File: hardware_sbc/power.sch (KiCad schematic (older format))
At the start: 49 parts, among them J6 Conn_01x02, J7 S2B-PH-K-S(LF)(SN), J8 Conn_01x01_Male, J9 0874380343, U10 MIC94164, U5 MP2636GR-P, U6 NCP133AMX150TCG

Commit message: Clean up bom and add config for KiBoM
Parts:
- D3, D4, D5: Part (none) -> 150060GS75000; Vendor 732-4971-1-ND -> (none); Vendorpart 150060GS75000 -> 732-4971-1-ND
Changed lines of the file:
@@
 F 2 "LED_SMD:LED_0603_1608Metric" H 6600 6850 50  0001 C CNN
 F 3 "~" H 6600 6850 50  0001 C CNN
-F 4 "732-4971-1-ND" H 6600 6850 50  0001 C CNN "Vendor"
-F 5 "150060GS75000" H 6593 6686 50  0001 C CNN "Vendorpart"
-F 6 "Wurth" H 6600 6850 50  0001 C CNN "Mfgr"
-F 7 "DNP" H 6600 6950 50  0000 C CNN "Populate"
+F 4 "732-4971-1-ND" H 6593 6686 50  0001 C CNN "Vendorpart"
+F 5 "Wurth" H 6600 6850 50  0001 C CNN "Mfgr"
+F 6 "DNP" H 6600 6950 50  0000 C CNN "Populate"
+F 7 "150060GS75000" H 6600 6850 50  0001 C CNN "Part"
 	1    6600 6850
 	-1   0    0    1
@@
 F 2 "LED_SMD:LED_0603_1608Metric" H 6600 7050 50  0001 C CNN
 F 3 "~" H 6600 7050 50  0001 C CNN
-F 4 "732-4971-1-ND" H 6600 7050 50  0001 C CNN "Vendor"
-F 5 "150060GS75000" H 6593 6795 50  0001 C CNN "Vendorpart"
-F 6 "Wurth" H 6600 7050 50  0001 C CNN "Mfgr"
-F 7 "DNP" H 6600 7150 50  0000 C CNN "Populate"
+F 4 "732-4971-1-ND" H 6593 6795 50  0001 C CNN "Vendorpart"
+F 5 "Wurth" H 6600 7050 50  0001 C CNN "Mfgr"
+F 6 "DNP" H 6600 7150 50  0000 C CNN "Populate"
+F 7 "150060GS75000" H 6600 7050 50  0001 C CNN "Part"
 	1    6600 7050
 	-1   0    0    1
@@
 F 2 "LED_SMD:LED_0603_1608Metric" H 6600 6650 50  0001 C CNN
 F 3 "~" H 6600 6650 50  0001 C CNN
-F 4 "732-4971-1-ND" H 6600 6650 50  0001 C CNN "Vendor"
-F 5 "150060GS75000" H 6593 6486 50  0001 C CNN "Vendorpart"
-F 6 "Wurth" H 6600 6650 50  0001 C CNN "Mfgr"
+F 4 "732-4971-1-ND" H 6593 6486 50  0001 C CNN "Vendorpart"
+F 5 "Wurth" H 6600 6650 50  0001 C CNN "Mfgr"
+F 6 "150060GS75000" H 6600 6650 50  0001 C CNN "Part"
 	1    6600 6650
 	-1   0    0    1

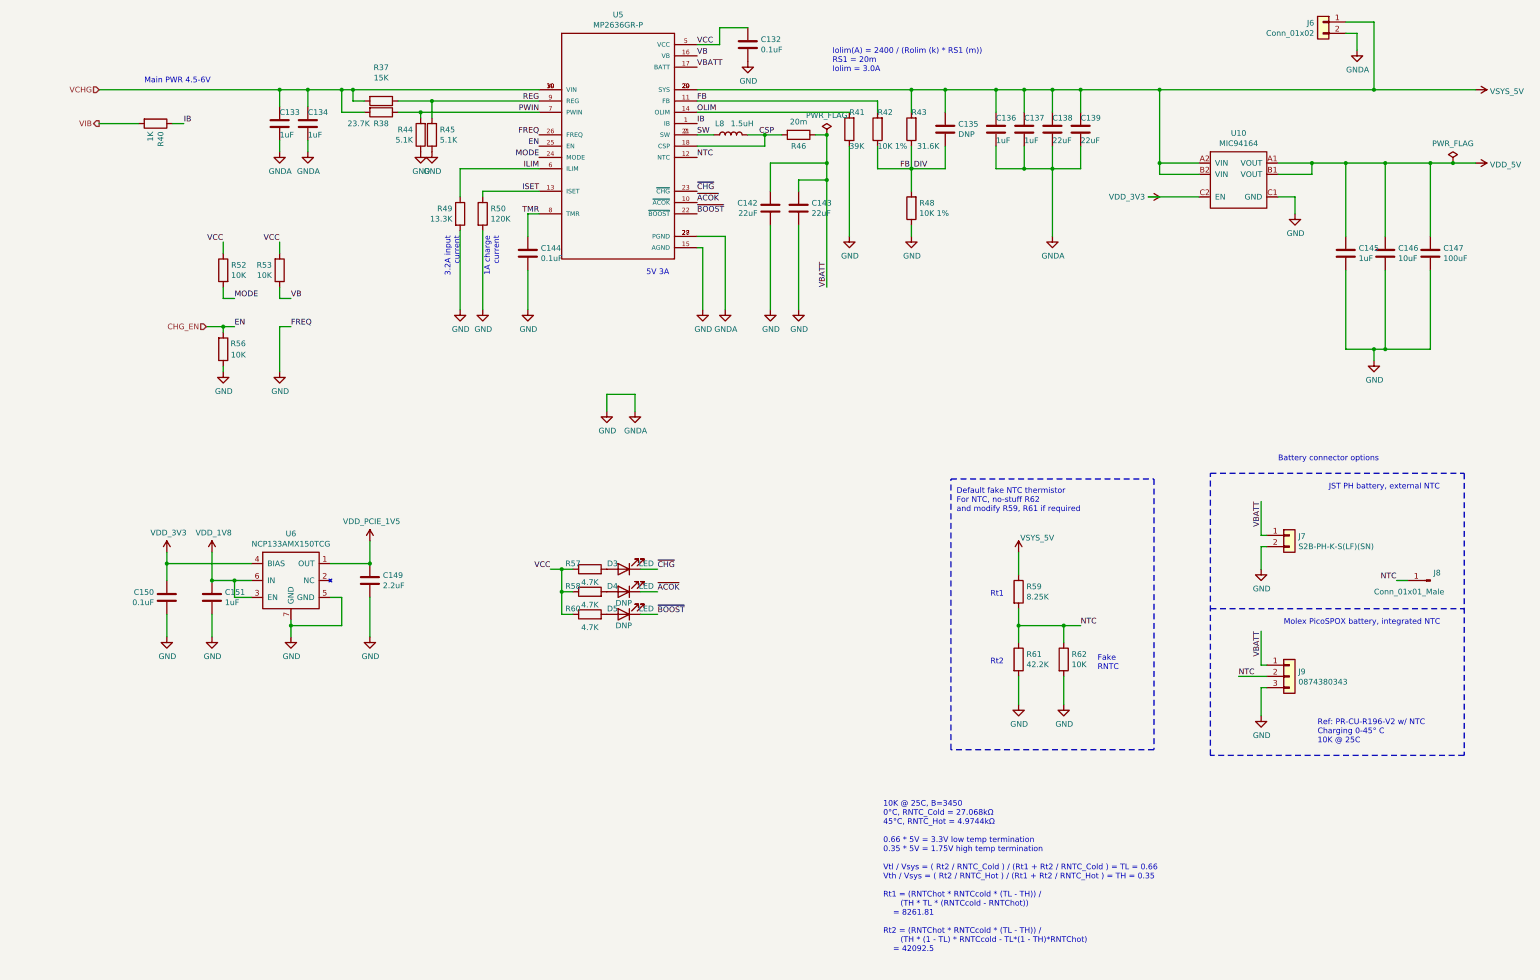
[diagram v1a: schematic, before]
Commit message: Add battery monitor and protection circuit
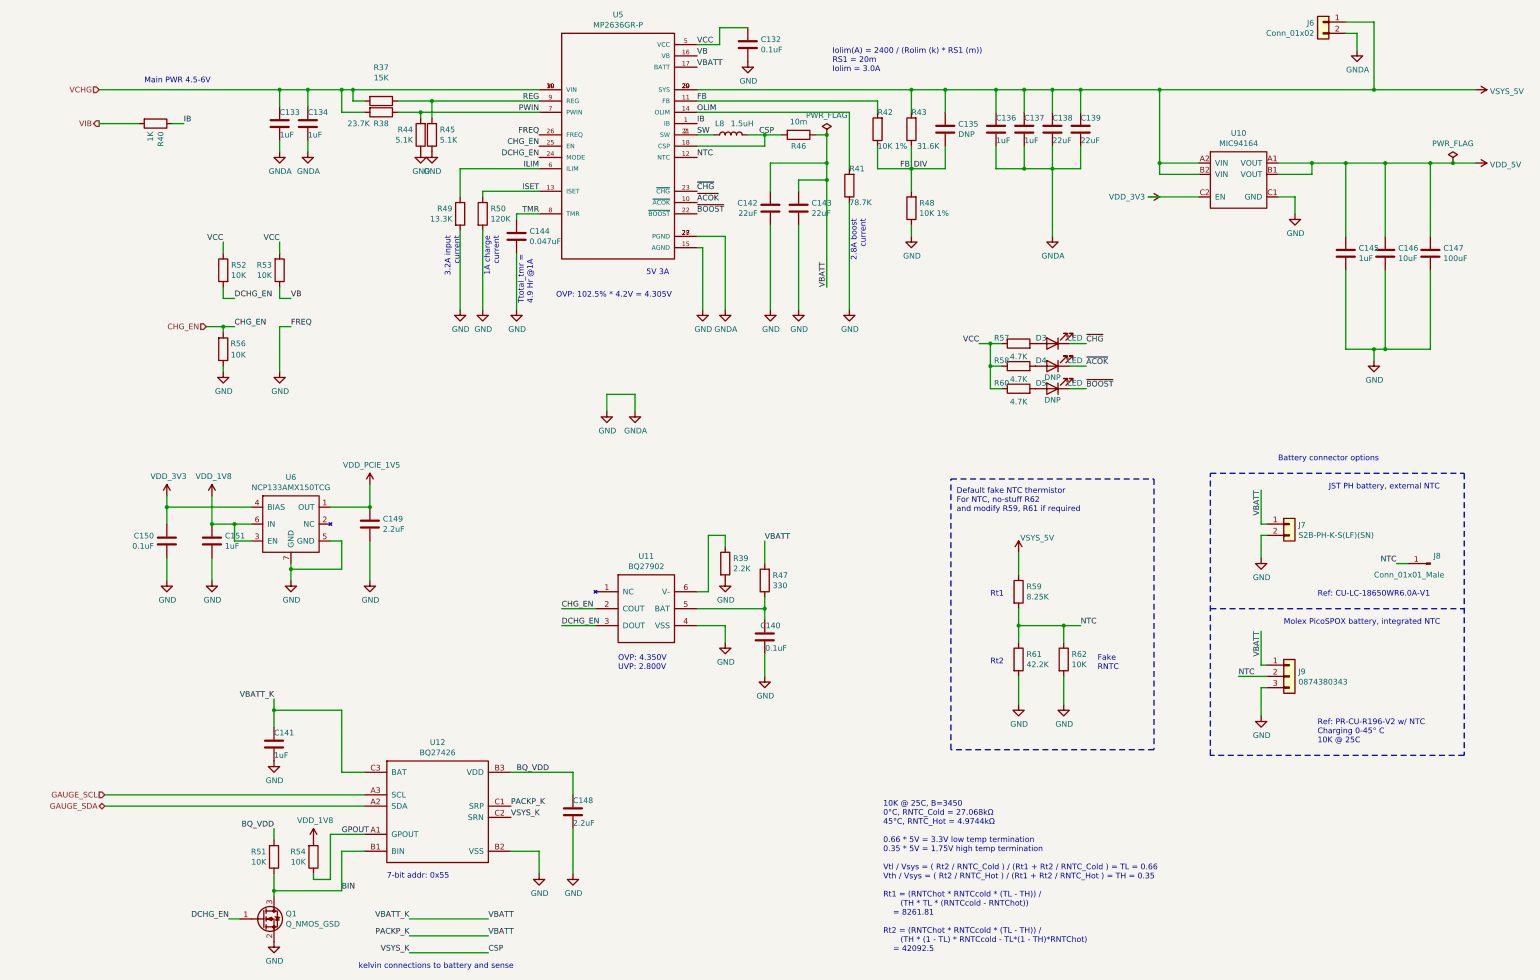
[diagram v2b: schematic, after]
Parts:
- added C140: 0.1uF, Capacitor_SMD:C_0201_0603Metric, symbol Device:C
- added C141: 1uF, Capacitor_SMD:C_0402_1005Metric, symbol Device:C
- added C148: 2.2uF, Capacitor_SMD:C_0201_0603Metric, symbol Device:C
- added Q1: Q_NMOS_GSD, Package_DFN_QFN:Diodes_DFN1006-3, symbol Device:Q_NMOS_GSD
- added R39: 2.2K, Resistor_SMD:R_0201_0603Metric, symbol Device:R
- added R47: 330, Resistor_SMD:R_0201_0603Metric, symbol Device:R
- added R51, R54: 10K, Resistor_SMD:R_0201_0603Metric, symbol Device:R
- added U11: BQ27902, Package_SON:WSON-6_1.5x1.5mm_P0.5mm, symbol mxenc:BQ279XX
- added U12: BQ27426, Package_BGA:BGA-9_1.6x1.6mm_Layout3x3_P0.5mm, symbol mxenc:BQ27426
- C144: value 0.1uF -> 0.047uF; Part GRM155R71E104KE14J -> GRM155R71A473KA01D; Vendorpart 490-14603-1-ND -> 490-1316-1-ND
- R41: value 39K -> 78.7K; Part RC0201FR-0739KL -> RC0201FR-0778R7L; Vendorpart YAG2641CT-ND -> YAG2803CT-ND
- R46: value 20m -> 10m; Part ERJ-8CWFR020V -> ERJ-8CWFR010V; Vendorpart P0.02BVCT-ND -> P0.01BVCT-ND
- R50: Part AC0201FR-07120KL -> AC0201FR-07240KL; Vendorpart YAG5150CT-ND -> YAG5179CT-ND
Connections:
- net CHG_EN: now also U11.2 (COUT)
- net CSP: now also U12.C2 (SRN)
- net GND: now also C140.2, C141.2, C148.2, Q1.2 (S), R39.2, U11.4 (VSS), U12.B2 (VSS)
- net VDD_1V8: now also R54.2
- net MODE renamed DCHG_EN
- net DCHG_EN: now also Q1.1 (G), U11.3 (DOUT)
- net VBATT renamed PACKP_K
- net PACKP_K: now also C141.1, R47.2, U12.C1 (SRP), U12.C3 (BAT)
- new net: C140.1, R47.1, U11.5 (BAT)
- new net: R39.1, U11.6 (V-)
- new net BIN: Q1.3 (D), R51.1, U12.B1 (BIN)
- new net BQ_VDD: C148.1, R51.2, U12.B3 (VDD)
- new net GAUGE_SCL: U12.A3 (SCL)
- new net GAUGE_SDA: U12.A2 (SDA)
- new net GPOUT: R54.1, U12.A1 (GPOUT)
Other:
- note added: "2.8A boost\ncurrent"
- note added: "7-bit addr: 0x55"
- note added: "OVP: 102.5% * 4.2V = 4.305V"
- note added: "OVP: 4.350V\nUVP: 2.800V"
- note added: "Ref: CU-LC-18650WR6.0A-V1"
- note added: "Ttotal_tmr =\n4.9 Hr @1A"
- note added: "kelvin connections to battery and sense"
- moved on the sheet: C144, C149, C150, C151, D3, D4, D5, J7, J8, R41, R57, R58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

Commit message: BOM and misc fixes for production of 0.9 boards
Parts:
- C132: Mfgrpart (none) -> GRM155R71E104KE14J; Part GRM155R71E104KE14J -> (none)
- C133, C134, C136, C137, C141, C145, C151: Mfgrpart (none) -> GRM155C81A105KA12D; Part GRM155C81A105KA12D -> (none)
- C138, C139, C142, C143: Mfgrpart (none) -> GRM188C80G226MEA0D; Part GRM188C80G226MEA0D -> (none)
- C140, C150: Mfgrpart (none) -> GRM033C80J104KE15D; Part GRM033C80J104KE15D -> (none)
- C144: Mfgrpart (none) -> GRM155R71A473KA01D; Part GRM155R71A473KA01D -> (none)
- C146: Mfgrpart (none) -> CL21X106KPYNNNE; Part CL21X106KPYNNNE -> (none)
- C147: Mfgrpart (none) -> GRM32EC70J107ME15L; Part GRM32EC70J107ME15L -> (none)
- C148: Mfgrpart (none) -> GRM033D80E225ME47D; Part GRM033D80E225ME47D -> (none)
- C149: Mfgrpart (none) -> GRM155C80J225ME95D; Part GRM155C80J225ME95D -> (none)
- D3, D4, D5: Mfgrpart (none) -> 150060GS75000; Part 150060GS75000 -> (none)
- J7: Mfgrpart (none) -> S2B-PH-K-S(LF)(SN); Part S2B-PH-K-S(LF)(SN) -> (none)
- J9: Mfgrpart (none) -> 0874380343; Part 0874380343 -> (none)
- L8: Mfgrpart (none) -> 74438357015; Part 74438357015 -> (none)
- Q1: Mfgrpart (none) -> NX7002BKMB; Part NX7002BKMB -> (none)
- R37: Mfgrpart (none) -> RC0201FR-0715KL; Part RC0201FR-0715KL -> (none)
- R38: Mfgrpart (none) -> RC0201FR-0723K7L; Part RC0201FR-0723K7L -> (none)
- R39: value 2.2K -> 2.2K 1%; Mfgr (none) -> Yageo; Mfgrpart (none) -> AC0201FR-072K2L; Vendorpart (none) -> YAG3422CT-ND
- R40: Mfgrpart (none) -> RC0402JR-071KL; Part RC0402JR-071KL -> (none)
- R41: Mfgrpart (none) -> RC0201FR-0778R7L; Part RC0201FR-0778R7L -> (none)
- R42, R48: Mfgrpart (none) -> RC0201FR-0710KL; Part RC0201FR-0710KL -> (none)
- R43: Mfgrpart (none) -> RC0201FR-0731K6L; Part RC0201FR-0731K6L -> (none)
- R44, R45: Mfgrpart (none) -> RC0201FR-075K1L; Part RC0201FR-075K1L -> (none)
- R46: Mfgrpart (none) -> ERJ-8CWFR010V; Part ERJ-8CWFR010V -> (none)
- R47: Mfgrpart (none) -> RC0201JR-07330RL; Part RC0201JR-07330RL -> (none)
- R49: Mfgrpart (none) -> RC0201FR-0713K3L; Part RC0201FR-0713K3L -> (none)
- R50: value 120K -> 240K; Mfgrpart (none) -> AC0201FR-07240KL; Part AC0201FR-07240KL -> (none)
- R51, R52, R53, R54, R56: Mfgrpart (none) -> ERJ-1GNJ103C; Part ERJ-1GNJ103C -> (none)
- R57, R58, R60: Mfgrpart (none) -> RC0201JR-074K7L; Part RC0201JR-074K7L -> (none)
- R59: Mfgrpart (none) -> RC0402FR-078K25L; Part RC0402FR-078K25L -> (none)
- R61: Mfgrpart (none) -> RC0402FR-0742K2L; Part RC0402FR-0742K2L -> (none)
- R62: Mfgrpart (none) -> ERJ-2GEJ103X; Part ERJ-2GEJ103X -> (none)
- U10: Mfgrpart (none) -> MIC94164YCS-TR; Part MIC94164YCS-TR -> (none)
- U11: value BQ27902 -> BQ29702; Mfgr (none) -> TI; Mfgrpart (none) -> BQ29702DSER; Vendorpart (none) -> 296-39945-1-ND
- U12: Mfgr (none) -> TI; Mfgrpart (none) -> BQ27426YZFR; Vendorpart (none) -> 296-43359-1-ND
- U5: Mfgrpart (none) -> MP2636GR-Z; Part MP2636GR-Z -> (none)
- U6: Mfgrpart (none) -> NCP133AMX150TCG; Part NCP133AMX150TCG -> (none)

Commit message: Don't stuff C125-127
These 3x 220uF caps are pulling down the 3v3 at boot. We need a
load switch in the next rev.
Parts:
- R50: Mfgrpart AC0201FR-07240KL -> RC0201FR-07240KL; Vendorpart YAG5179CT-ND -> YAG2527TR-ND
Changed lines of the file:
@@
 F 2 "Resistor_SMD:R_0201_0603Metric" V 5280 3500 50  0001 C CNN
 F 3 "~" H 5350 3500 50  0001 C CNN
-F 4 "YAG5179CT-ND" H 5420 3409 50  0001 L CNN "Vendorpart"
+F 4 "YAG2527TR-ND" H 5420 3409 50  0001 L CNN "Vendorpart"
 F 5 "Yageo" H 5350 3500 50  0001 C CNN "Mfgr"
 F 6 "" H 5350 3500 50  0001 C CNN "Part"
-F 7 "AC0201FR-07240KL" H 5350 3500 50  0001 C CNN "Mfgrpart"
+F 7 "RC0201FR-07240KL" H 5350 3500 50  0001 C CNN "Mfgrpart"
 	1    5350 3500
 	1    0    0    -1
@@
 P 3850 9050
 AR Path="/5D31363C/5EEEE00F" Ref="#PWR?"  Part="1"
-AR Path="/5DC6F4F1/5EEEE00F" Ref="#PWR?"  Part="1"
-F 0 "#PWR?" H 3850 8900 50  0001 C CNN
+AR Path="/5DC6F4F1/5EEEE00F" Ref="#PWR0234"  Part="1"
+F 0 "#PWR0234" H 3850 8900 50  0001 C CNN
 F 1 "VDD_1V8" H 3865 9223 50  0000 C CNN
 F 2 "" H 3850 9050 50  0001 C CNN

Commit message: Update BoM and add some errata notes for v0.9 builds moving forward
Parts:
- Q1: Populate (none) -> DNP
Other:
- note added: "See rework notes:\nhttps://github.com/groupgets/kimchi-micro/issues/5"
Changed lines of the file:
@@
 F 6 "" H 3400 9750 50  0001 C CNN "Part"
 F 7 "NX7002BKMB" H 3400 9750 50  0001 C CNN "Mfgrpart"
+F 8 "DNP" H 3700 9600 50  0000 C CNN "Populate"
 	1    3400 9750
 	1    0    0    -1
@@
 Text Notes 5800 4300 1    50   ~ 0
 Ttotal_tmr =\n4.9 Hr @1A
+Text Notes 1150 9550 0    50   ~ 0
+See rework notes:\nhttps://github.com/groupgets/kimchi-micro/issues/5
 $EndSCHEMATC
